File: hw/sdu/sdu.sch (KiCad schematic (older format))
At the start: 54 parts, among them J1 INTERFACE, J2 SWD, Q1 BC847, Q2 BC857, Q3 BC857, Q4 BC857, Q5 BC847, Q6 BC847, Q7 BC847, U1 TS1117BCW33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

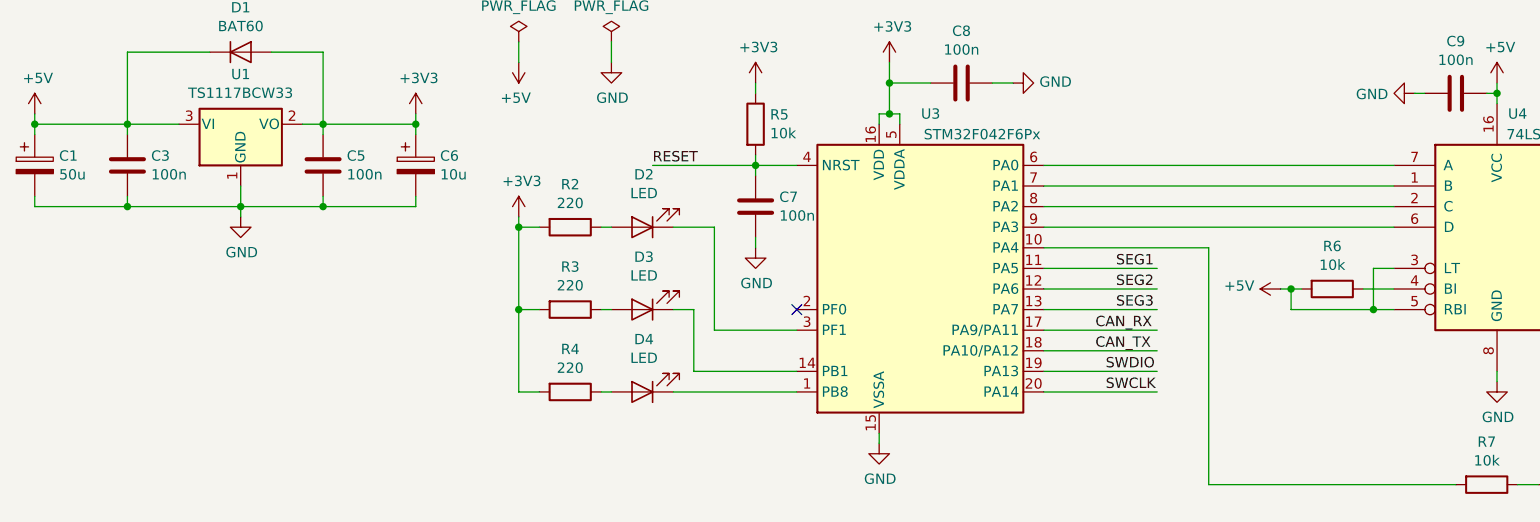
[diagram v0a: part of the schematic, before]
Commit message: Added HMI and SDU boards
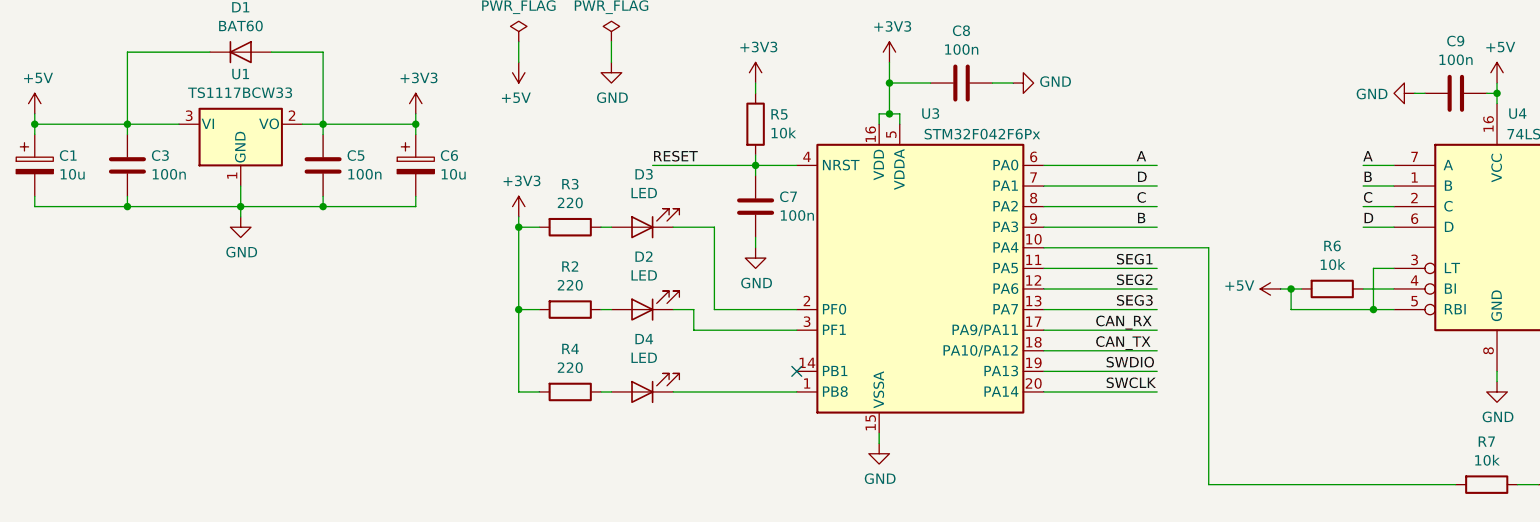
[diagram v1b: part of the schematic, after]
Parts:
- C1: value 50u -> 10u; footprint Capacitor_SMD:CP_Elec_6.3x7.7 -> Capacitor_SMD:C_0805_2012Metric
- D2, D3, D4: footprint LED_SMD:LED_1206_3216Metric -> LED_THT:LED_D5.0mm
- J1: footprint Connector_Dsub:DSUB-9_Female_Vertical_P2.77x2.84mm -> Connector_Dsub:DSUB-9_Female_Vertical_P2.77x2.84mm_MountingHoles
- J2: footprint Connector_PinSocket_2.54mm:PinSocket_1x05_P2.54mm_Horizontal -> Connector_PinHeader_2.54mm:PinHeader_1x05_P2.54mm_Horizontal
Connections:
- net labels added: A, B, C, D
- wire segments 218 -> 222
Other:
- moved on the sheet: D2, D3, R2, R3
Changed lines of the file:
@@
 F 0 "D4" H 3592 2195 50  0000 C CNN
 F 1 "LED" H 3592 2286 50  0000 C CNN
-F 2 "LED_SMD:LED_1206_3216Metric" H 3600 2450 50  0001 C CNN
+F 2 "LED_THT:LED_D5.0mm" H 3600 2450 50  0001 C CNN
 F 3 "~" H 3600 2450 50  0001 C CNN
 	1    3600 2450
@@
 L Device:LED D3
 U 1 1 5E082BDF
+P 3600 1650
+F 0 "D3" H 3592 1395 50  0000 C CNN
+F 1 "LED" H 3592 1486 50  0000 C CNN
+F 2 "LED_THT:LED_D5.0mm" H 3600 1650 50  0001 C CNN
+F 3 "~" H 3600 1650 50  0001 C CNN
+	1    3600 1650
+	-1   0    0    1
+$EndComp
+$Comp
+L Device:R R3
+U 1 1 5E082BE6
+P 3250 1650
+F 0 "R3" V 3043 1650 50  0000 C CNN
+F 1 "220" V 3134 1650 50  0000 C CNN
+F 2 "Resistor_SMD:R_0805_2012Metric" V 3180 1650 50  0001 C CNN
+F 3 "~" H 3250 1650 50  0001 C CNN
+	1    3250 1650
+	0    1    1    0
+$EndComp
+Wire Wire Line
+	3400 1650 3450 1650
+$Comp
+L Device:LED D2
+U 1 1 5E085DA1
 P 3600 2050
-F 0 "D3" H 3592 1795 50  0000 C CNN
+F 0 "D2" H 3592 1795 50  0000 C CNN
 F 1 "LED" H 3592 1886 50  0000 C CNN
-F 2 "LED_SMD:LED_1206_3216Metric" H 3600 2050 50  0001 C CNN
+F 2 "LED_THT:LED_D5.0mm" H 3600 2050 50  0001 C CNN
 F 3 "~" H 3600 2050 50  0001 C CNN
 	1    3600 2050
@@
 $EndComp
 $Comp
-L Device:R R3
-U 1 1 5E082BE6
+L Device:R R2
+U 1 1 5E085DA8
 P 3250 2050
-F 0 "R3" V 3043 2050 50  0000 C CNN
+F 0 "R2" V 3043 2050 50  0000 C CNN
 F 1 "220" V 3134 2050 50  0000 C CNN
 F 2 "Resistor_SMD:R_0805_2012Metric" V 3180 2050 50  0001 C CNN
@@
 Wire Wire Line
 	3400 2050 3450 2050
-$Comp
-L Device:LED D2
-U 1 1 5E085DA1
-P 3600 1650
-F 0 "D2" H 3592 1395 50  0000 C CNN
-F 1 "LED" H 3592 1486 50  0000 C CNN
-F 2 "LED_SMD:LED_1206_3216Metric" H 3600 1650 50  0001 C CNN
-F 3 "~" H 3600 1650 50  0001 C CNN
-	1    3600 1650
-	-1   0    0    1
-$EndComp
-$Comp
-L Device:R R2
-U 1 1 5E085DA8
-P 3250 1650
-F 0 "R2" V 3043 1650 50  0000 C CNN
-F 1 "220" V 3134 1650 50  0000 C CNN
-F 2 "Resistor_SMD:R_0805_2012Metric" V 3180 1650 50  0001 C CNN
-F 3 "~" H 3250 1650 50  0001 C CNN
-	1    3250 1650
-	0    1    1    0
-$EndComp
-Wire Wire Line
-	3400 1650 3450 1650
 Wire Wire Line
 	3750 2050 3850 2050
-Wire Wire Line
-	3850 2050 3850 2350
-Wire Wire Line
-	3850 2350 4350 2350
-Wire Wire Line
-	4350 2150 3950 2150
-Wire Wire Line
-	3950 2150 3950 1650
 Wire Wire Line
 	3950 1650 3750 1650
@@
 F 0 "J1" H 5150 7500 50  0000 L CNN
 F 1 "INTERFACE" V 5250 6800 50  0000 L CNN
-F 2 "Connector_Dsub:DSUB-9_Female_Vertical_P2.77x2.84mm" H 5050 7000 50  0001 C CNN
+F 2 "Connector_Dsub:DSUB-9_Female_Vertical_P2.77x2.84mm_MountingHoles" H 5050 7000 50  0001 C CNN
 F 3 " ~" H 5050 7000 50  0001 C CNN
 	1    5050 7000
@@
 F 0 "J2" H 6730 7142 50  0000 L CNN
 F 1 "SWD" H 6730 7051 50  0000 L CNN
-F 2 "Connector_PinSocket_2.54mm:PinSocket_1x05_P2.54mm_Horizontal" H 6650 7100 50  0001 C CNN
+F 2 "Connector_PinHeader_2.54mm:PinHeader_1x05_P2.54mm_Horizontal" H 6650 7100 50  0001 C CNN
 F 3 "~" H 6650 7100 50  0001 C CNN
 	1    6650 7100
@@
 P 650 1350
 F 0 "C1" H 768 1396 50  0000 L CNN
-F 1 "50u" H 768 1305 50  0000 L CNN
-F 2 "Capacitor_SMD:CP_Elec_6.3x7.7" H 688 1200 50  0001 C CNN
+F 1 "10u" H 768 1305 50  0000 L CNN
+F 2 "Capacitor_SMD:C_0805_2012Metric" H 688 1200 50  0001 C CNN
 F 3 "~" H 650 1350 50  0001 C CNN
 	1    650  1350
@@
 	8750 2050 9000 2050
 Connection ~ 9000 2050
-Wire Wire Line
-	5550 1350 7250 1350
-Wire Wire Line
-	5550 1450 7250 1450
-Wire Wire Line
-	5550 1550 7250 1550
-Wire Wire Line
-	5550 1650 7250 1650
 $Comp
 L Device:R R7
@@
 Wire Wire Line
 	9000 3900 9000 5750
-NoConn ~ 4350 2050
 $Comp
 L Device:C C9
@@
 	10800 5350 10800 5300
 Connection ~ 10800 5350
+Wire Wire Line
+	7250 1350 7100 1350
+Text Label 7100 1350 0    50   ~ 0
+A
+Wire Wire Line
+	7250 1450 7100 1450
+Text Label 7100 1450 0    50   ~ 0
+B
+Wire Wire Line
+	7250 1550 7100 1550
+Text Label 7100 1550 0    50   ~ 0
+C
+Wire Wire Line
+	7250 1650 7100 1650
+Text Label 7100 1650 0    50   ~ 0
+D
+Wire Wire Line
+	5550 1650 6100 1650
+Text Label 6000 1350 0    50   ~ 0
+A
+Wire Wire Line
+	5550 1550 6100 1550
+Text Label 6000 1550 0    50   ~ 0
+C
+Wire Wire Line
+	5550 1450 6100 1450
+Wire Wire Line
+	5550 1350 6100 1350
+Text Label 6000 1650 0    50   ~ 0
+B
+Text Label 6000 1450 0    50   ~ 0
+D
+Wire Wire Line
+	3950 1650 3950 2050
+Wire Wire Line
+	3950 2050 4350 2050
+NoConn ~ 4350 2350
+Wire Wire Line
+	4350 2150 3850 2150
+Wire Wire Line
+	3850 2150 3850 2050
 $EndSCHEMATC

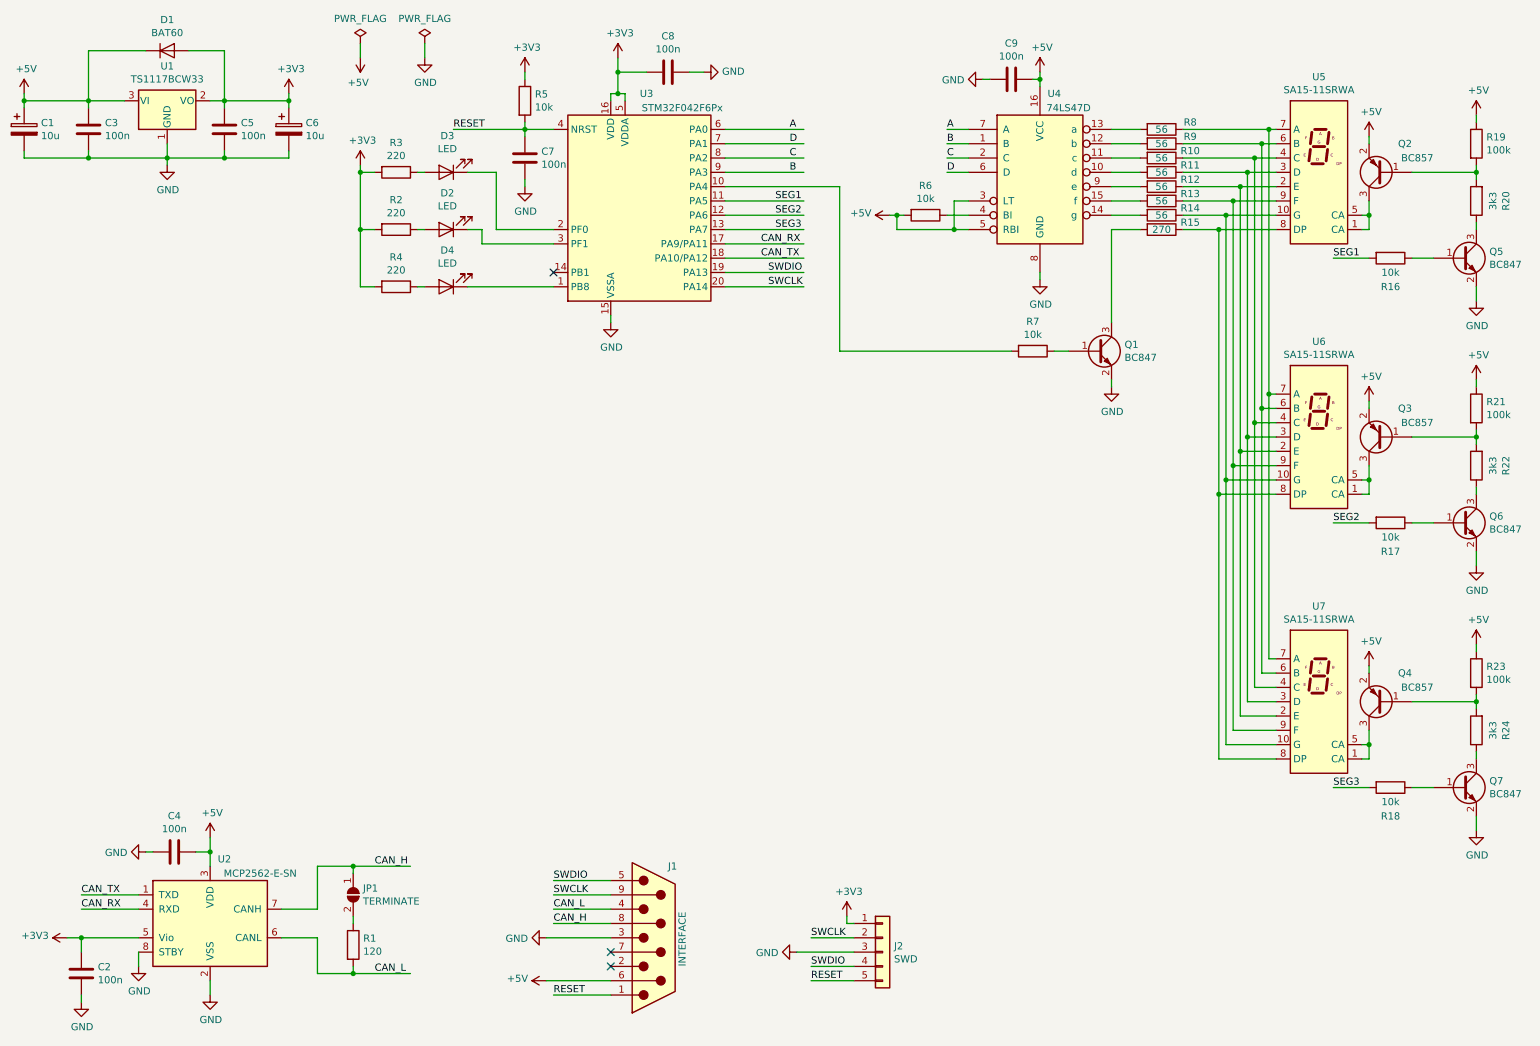
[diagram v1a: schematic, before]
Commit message: Added crystal for all can equipped boards
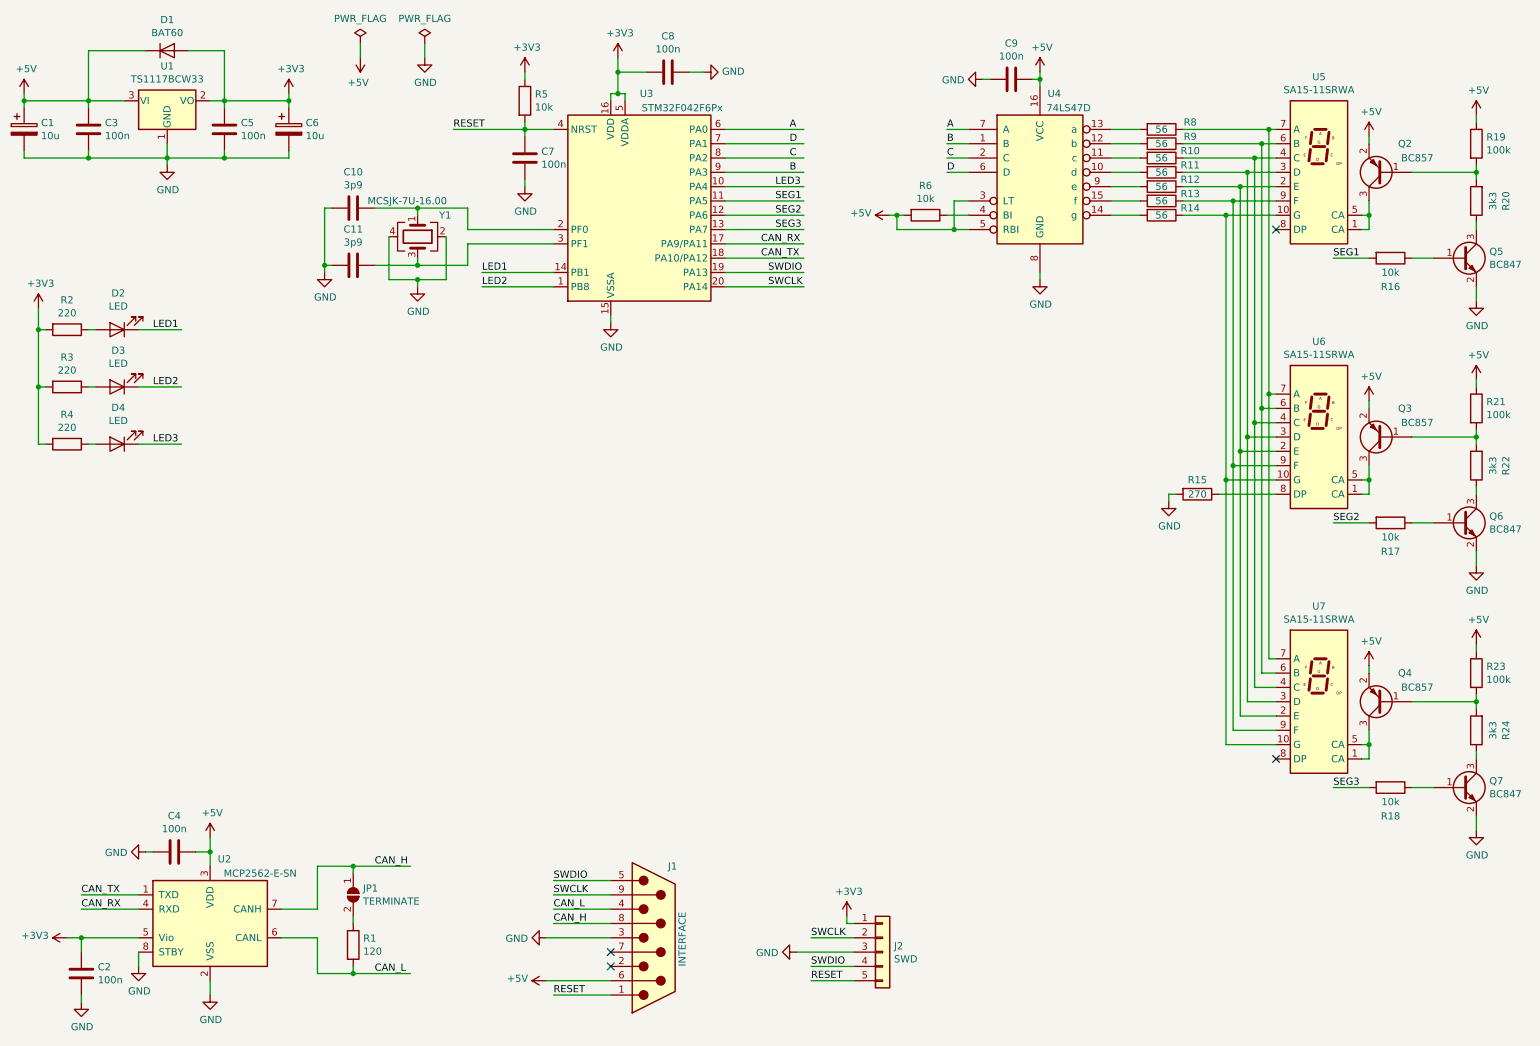
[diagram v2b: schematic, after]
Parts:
- removed Q1: BC847, Package_TO_SOT_SMD:SOT-23, symbol Transistor_BJT:BC847
- removed R7: 10k, Resistor_SMD:R_0805_2012Metric, symbol Device:R
- added C10, C11: 3p9, Capacitor_SMD:C_0805_2012Metric, symbol Device:C
- added Y1: MCSJK-7U-16.00, Crystal:Crystal_SMD_3225-4Pin_3.2x2.5mm, symbol Device:Crystal_GND24
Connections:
- net labels added: LED1, LED2, LED3
- wire segments 222 -> 230
- no-connect marks 3 -> 4
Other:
- moved on the sheet: D2, D3, D4, R15, R2, R3, R4

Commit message: Updated SDU board
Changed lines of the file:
@@
 LED3
 Wire Wire Line
-	4350 2350 3850 2350
-Text Label 3850 2350 0    50   ~ 0
+	6100 1750 5550 1750
+Text Label 5900 1750 0    50   ~ 0
 LED1
 Wire Wire Line
@@
 LED2
 Wire Wire Line
-	5550 1750 6100 1750
-Text Label 5900 1750 0    50   ~ 0
+	3850 2350 4350 2350
+Text Label 3850 2350 0    50   ~ 0
 LED3
 $EndSCHEMATC
